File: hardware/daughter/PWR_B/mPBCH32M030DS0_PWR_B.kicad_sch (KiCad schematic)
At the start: 0 parts

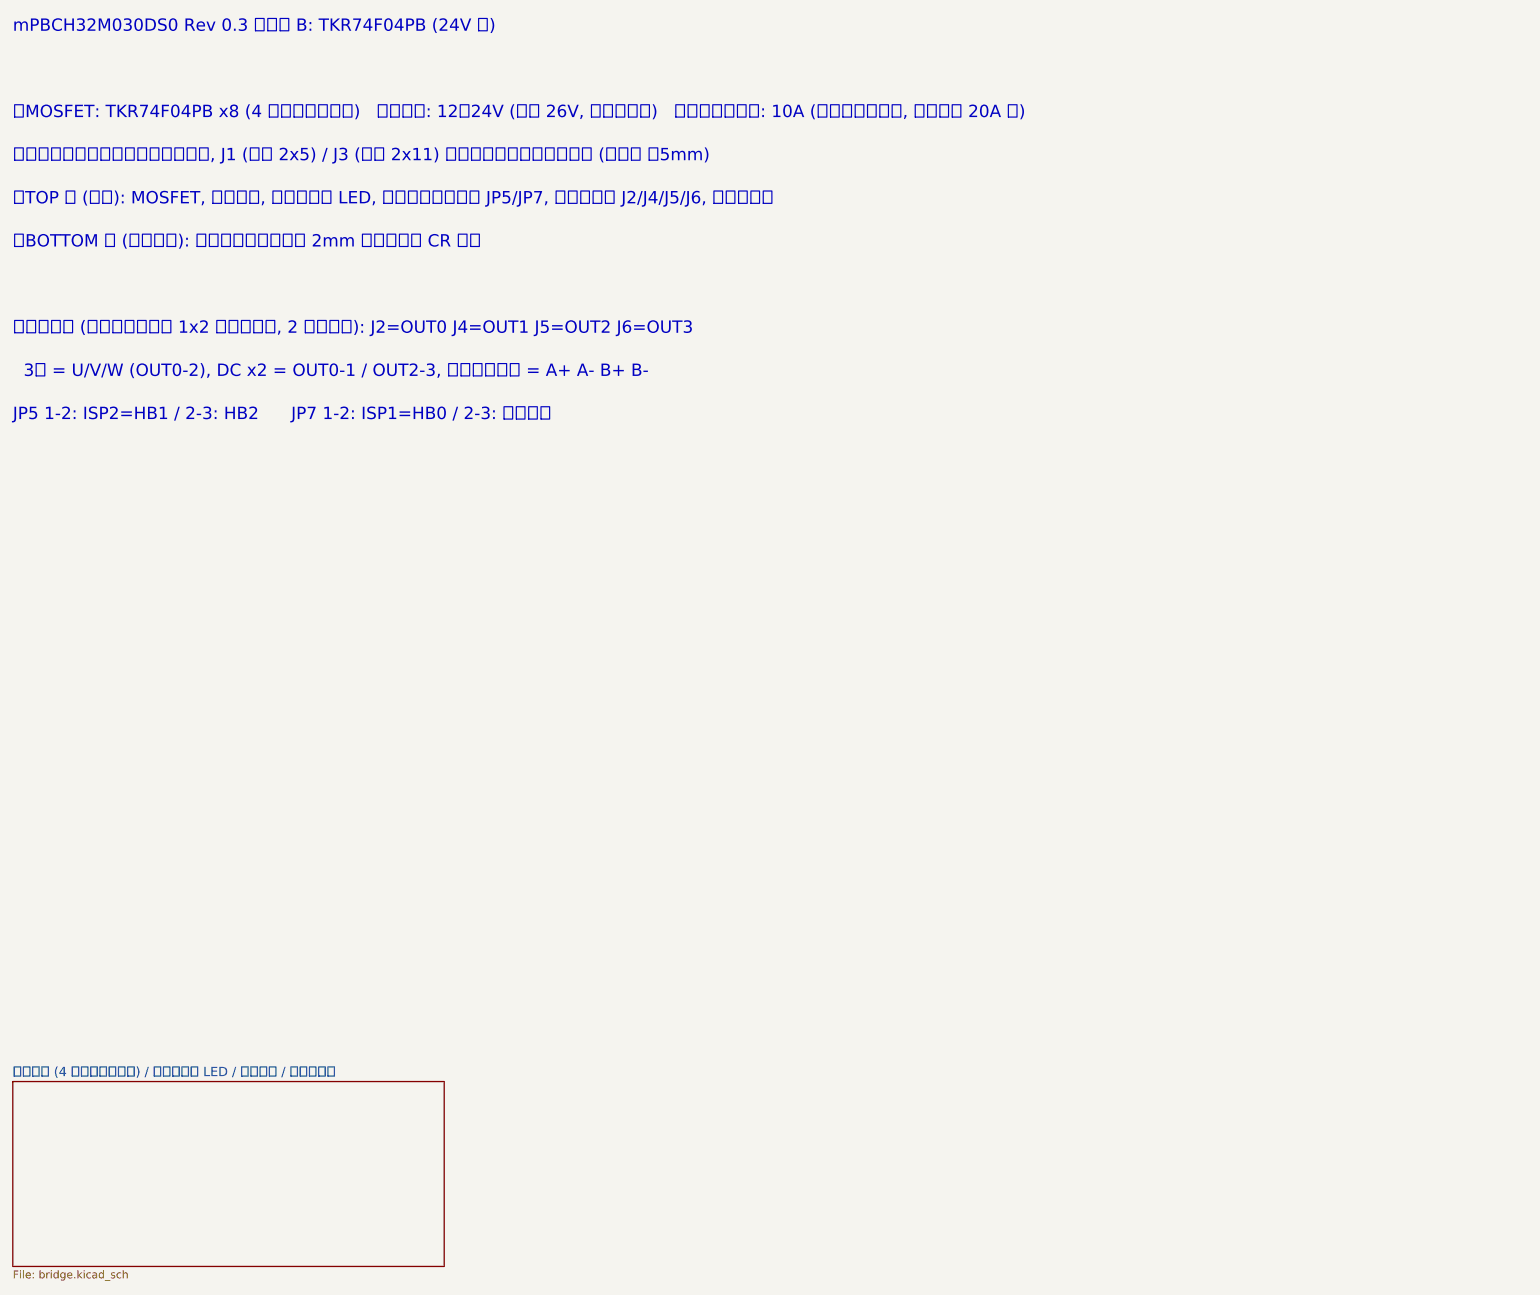
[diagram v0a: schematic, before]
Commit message: Rev 0.4: DIP-42 MCU module + power boards A/B/C (KiCad 8)
- MCU module: 20.32 x 53.34mm (8 x 21 grid), DIP-42 (0.6in rows), fits
  an 82 x 52mm breadboard. Headers can be fitted from either side;
  signal names on bottom silk. All LEDs (power, status, 8 gate LEDs) on
  the module top.
- Power boards take the module in two 1x21 sockets (left/right
  symmetric mating). FETs/shunts on the heatsink side, no LEDs.
  Voltage-dependent parts (TVS, OVP divider, bulk caps, BEMF divider)
  moved to the power boards. Breakout board D removed.
  A/C: 20.32 x 71.94mm, B (TO-263 x8): 40.64 x 66.94mm.
- Capacitors re-selected for realistic size vs voltage/capacitance
  (4.7uF 1608, 10uF/25V 2012, 10uF/50V 1206, 4.7nF/100V 1608, low
  profile electrolytics).
- Schematics and boards generated in KiCad 8 format; netlists verified
  with KiCad 8.0.9.
- Layout pipeline: Freerouting bridge (parallel), second pass, early
  repair before pours, island-aware maze repair, DRC via kicad-cli.
- DRC: power boards A/B/C have 0 unconnected / 0 electrical errors.
  The MCU module still has unrouted connections (work in progress).

Co-Authored-By: Claude Opus 5.5 <noreply@anthropic.com>
Claude-Session: https://claude.ai/code/session_01LENFjjhDfYjJZV1NWhB9uV
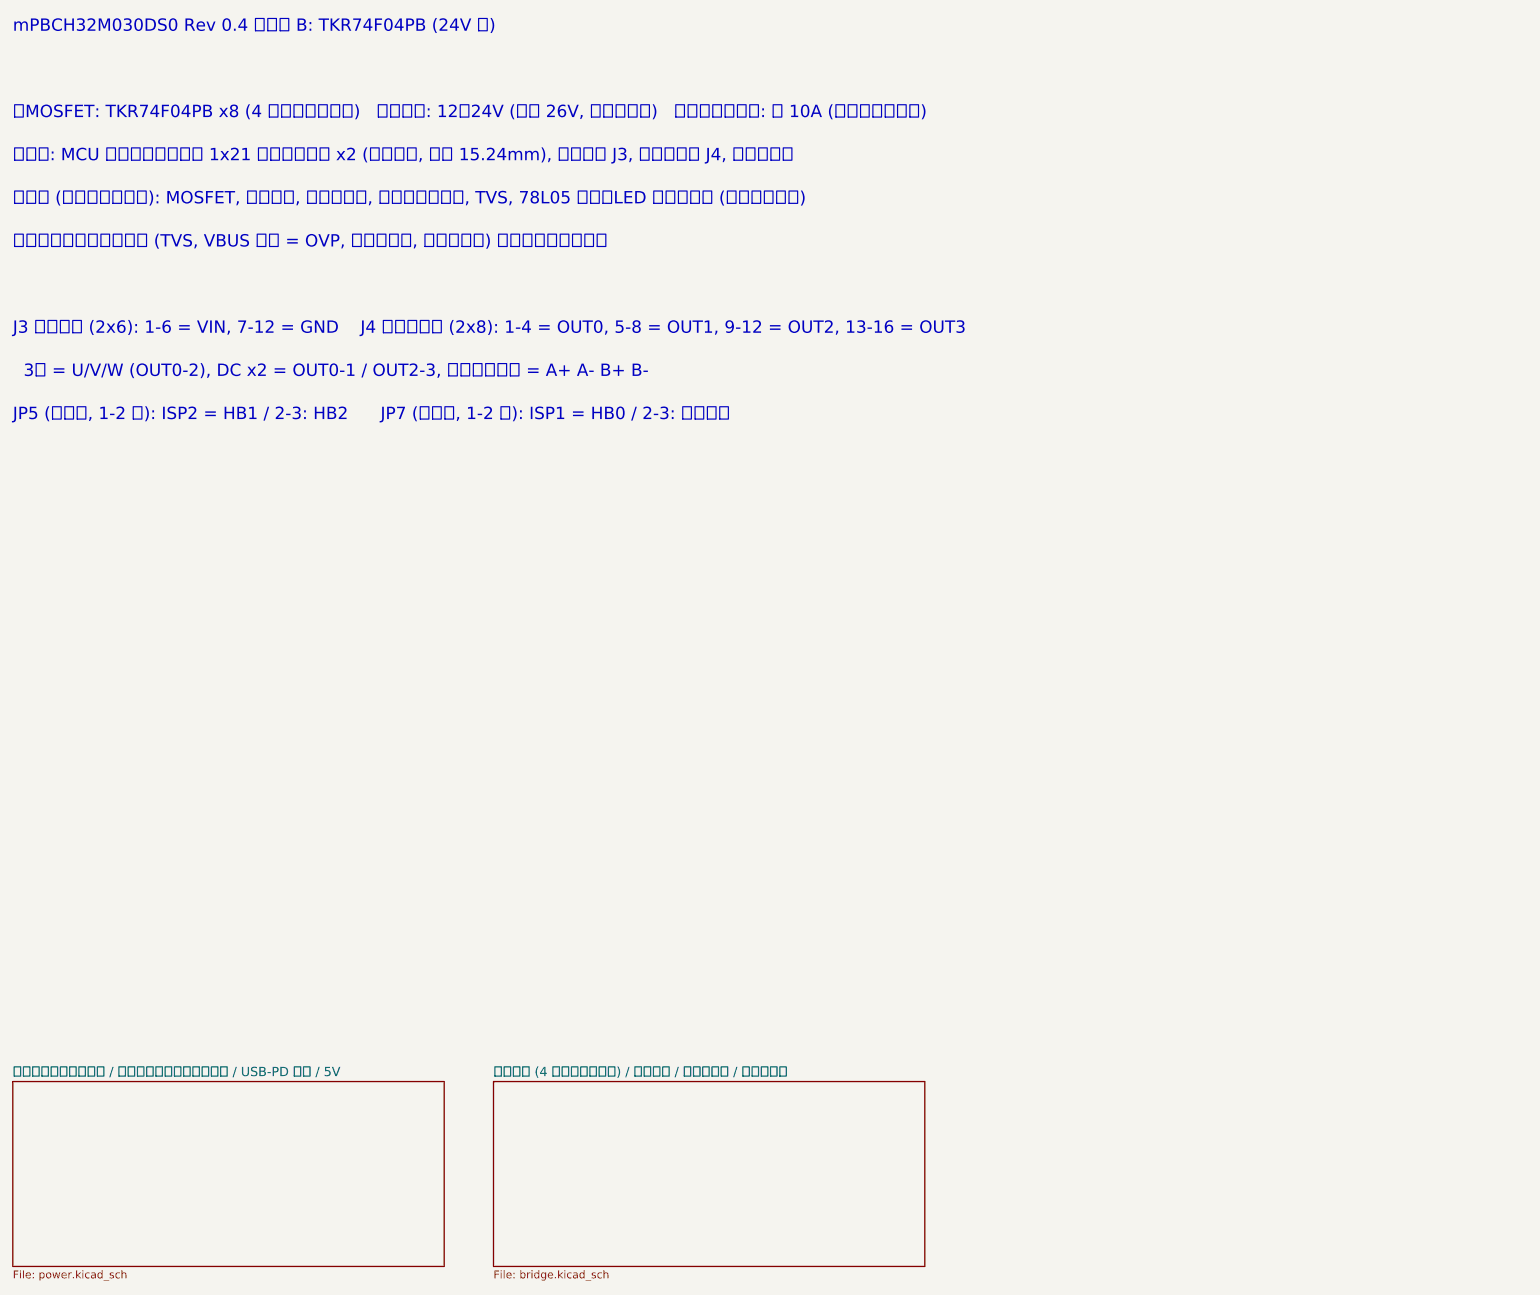
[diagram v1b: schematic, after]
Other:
- sheet パワー段 (4 ハーフブリッジ) / ゲート確認 LED / シャント / モータ出力 renamed パワー段 (4 ハーフブリッジ) / シャント / 相電圧分圧 / モータ出力
- added sheet モジュール用ソケット / 電源入力・理想ダイオード / USB-PD 経路 / 5V (power.kicad_sch)
- note added: "J3 電源入力 (2x6): 1-6 = VIN, 7-12 = GND J4 モータ出力 (2x8): 1-4 = OUT0, 5-8 = OUT1, 9-12 = OUT2, 13-16 = OUT3"
- note added: "JP5 (はんだ, 1-2 済): ISP2 = HB1 / 2-3: HB2 JP7 (はんだ, 1-2 済): ISP1 = HB0 / 2-3: バス電流"
- note added: "mPBCH32M030DS0 Rev 0.4 子基板 B: TKR74F04PB (24V 系)"
- note added: "・MOSFET: TKR74F04PB x8 (4 ハーフブリッジ) 入力電圧: 12〜24V (上限 26V, 安定化電源) 出力電流の目安: 約 10A (ピンヘッダ律速)"
- note added: "・上面: MCU モジュールを挿す 1x21 ピンソケット x2 (左右対称, 列間 15.24mm), 電源入力 J3, モータ出力 J4, バルク容量"
- note added: "・下面 (ヒートシンク側): MOSFET, シャント, ゲート抵抗, 理想ダイオード, TVS, 78L05 など。LED は置かない (モジュール側)"
- note added: "・電圧系に依存する部品 (TVS, VBUS 分圧 = OVP, バルク容量, 相電圧分圧) はこの基板で決める"
- note removed: "JP5 1-2: ISP2=HB1 / 2-3: HB2 JP7 1-2: ISP1=HB0 / 2-3: バス電流"
- note removed: "mPBCH32M030DS0 Rev 0.3 子基板 B: TKR74F04PB (24V 系)"
- note removed: "モータ出力 (各レッグ直近の 1x2 ピンヘッダ, 2 ピン並列): J2=OUT0 J4=OUT1 J5=OUT2 J6=OUT3"
- note removed: "・BOTTOM 面 (主基板側): ピンソケットと高さ 2mm 以下の小型 CR のみ"
- note removed: "・MOSFET: TKR74F04PB x8 (4 ハーフブリッジ) 入力電圧: 12〜24V (最大 26V, 安定化電源) 出力電流の目安: 10A (ピンヘッダ律速, 直付けで 20A 級)"
- note removed: "・TOP 面 (外側): MOSFET, シャント, ゲート確認 LED, 電流チャネル選択 JP5/JP7, モータ出力 J2/J4/J5/J6, バルク容量"
- note removed: "・主基板と裏面同士を向かい合わせ, J1 (電源 2x5) / J3 (信号 2x11) の裏面ピンソケットで接続 (基板間 約5mm)"
- title: mPBCH32M030DS0 Power daughter board B (TKR74F04PB) -> mPBCH32M030DS0 power board B (TKR74F04PB)
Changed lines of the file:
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@@
-(kicad_sch (version 20230121) (generator eeschema)
+(kicad_sch (version 20231120) (generator "eeschema") (generator_version "8.0")
 (paper "A3")
-(title_block (title "mPBCH32M030DS0 Power daughter board B (TKR74F04PB)") (date "2026-09-25") (rev "0.3") (company "ghostinkoma") (comment 1 "トップシート / 仕様概要") (comment 2 "個人利用可 (クレジット表示必須) / 商用利用は要連絡 / 無保証  -  LICENSE 参照"))
-(text "mPBCH32M030DS0 Rev 0.3 子基板 B: TKR74F04PB (24V 系)" (at 20 30 0) (effects (font (size 2 2)) (justify left bottom)))
-(text "" (at 20 37 0) (effects (font (size 2 2)) (justify left bottom)))
-(text "・MOSFET: TKR74F04PB x8 (4 ハーフブリッジ)   入力電圧: 12〜24V (最大 26V, 安定化電源)   出力電流の目安: 10A (ピンヘッダ律速, 直付けで 20A 級)" (at 20 44 0) (effects (font (size 2 2)) (justify left bottom)))
-(text "・主基板と裏面同士を向かい合わせ, J1 (電源 2x5) / J3 (信号 2x11) の裏面ピンソケットで接続 (基板間 約5mm)" (at 20 51 0) (effects (font (size 2 2)) (justify left bottom)))
-(text "・TOP 面 (外側): MOSFET, シャント, ゲート確認 LED, 電流チャネル選択 JP5/JP7, モータ出力 J2/J4/J5/J6, バルク容量" (at 20 58 0) (effects (font (size 2 2)) (justify left bottom)))
-(text "・BOTTOM 面 (主基板側): ピンソケットと高さ 2mm 以下の小型 CR のみ" (at 20 65 0) (effects (font (size 2 2)) (justify left bottom)))
-(text "" (at 20 72 0) (effects (font (size 2 2)) (justify left bottom)))
-(text "モータ出力 (各レッグ直近の 1x2 ピンヘッダ, 2 ピン並列): J2=OUT0 J4=OUT1 J5=OUT2 J6=OUT3" (at 20 79 0) (effects (font (size 2 2)) (justify left bottom)))
-(text "  3相 = U/V/W (OUT0-2), DC x2 = OUT0-1 / OUT2-3, ステッピング = A+ A- B+ B-" (at 20 86 0) (effects (font (size 2 2)) (justify left bottom)))
-(text "JP5 1-2: ISP2=HB1 / 2-3: HB2      JP7 1-2: ISP1=HB0 / 2-3: バス電流" (at 20 93 0) (effects (font (size 2 2)) (justify left bottom)))
-(sheet (at 20 200) (size 70 30) (fields_autoplaced) (stroke (width 0.1524) (type solid)) (fill (color 0 0 0 0.0000))
-(property "Sheetname" "パワー段 (4 ハーフブリッジ) / ゲート確認 LED / シャント / モータ出力" (at 20 199.3 0) (effects (font (size 1.5 1.5)) (justify left bottom)))
-(property "Sheetfile" "bridge.kicad_sch" (at 20 230.6 0) (effects (font (size 1.27 1.27)) (justify left top)))
+(title_block (title "mPBCH32M030DS0 power board B (TKR74F04PB)") (date "2026-09-26") (rev "0.4") (company "ghostinkoma") (comment 1 "トップシート / 仕様概要") (comment 2 "個人利用可 (クレジット表示必須) / 商用利用は要連絡 / 無保証  -  LICENSE 参照"))
+(text "mPBCH32M030DS0 Rev 0.4 子基板 B: TKR74F04PB (24V 系)" (exclude_from_sim no) (at 20 30 0) (effects (font (size 2 2)) (justify left bottom)))
+(text "" (exclude_from_sim no) (at 20 37 0) (effects (font (size 2 2)) (justify left bottom)))
+(text "・MOSFET: TKR74F04PB x8 (4 ハーフブリッジ)   入力電圧: 12〜24V (上限 26V, 安定化電源)   出力電流の目安: 約 10A (ピンヘッダ律速)" (exclude_from_sim no) (at 20 44 0) (effects (font (size 2 2)) (justify left bottom)))
+(text "・上面: MCU モジュールを挿す 1x21 ピンソケット x2 (左右対称, 列間 15.24mm), 電源入力 J3, モータ出力 J4, バルク容量" (exclude_from_sim no) (at 20 51 0) (effects (font (size 2 2)) (justify left bottom)))
+(text "・下面 (ヒートシンク側): MOSFET, シャント, ゲート抵抗, 理想ダイオード, TVS, 78L05 など。LED は置かない (モジュール側)" (exclude_from_sim no) (at 20 58 0) (effects (font (size 2 2)) (justify left bottom)))
+(text "・電圧系に依存する部品 (TVS, VBUS 分圧 = OVP, バルク容量, 相電圧分圧) はこの基板で決める" (exclude_from_sim no) (at 20 65 0) (effects (font (size 2 2)) (justify left bottom)))
+(text "" (exclude_from_sim no) (at 20 72 0) (effects (font (size 2 2)) (justify left bottom)))
+(text "J3 電源入力 (2x6): 1-6 = VIN, 7-12 = GND    J4 モータ出力 (2x8): 1-4 = OUT0, 5-8 = OUT1, 9-12 = OUT2, 13-16 = OUT3" (exclude_from_sim no) (at 20 79 0) (effects (font (size 2 2)) (justify left bottom)))
+(text "  3相 = U/V/W (OUT0-2), DC x2 = OUT0-1 / OUT2-3, ステッピング = A+ A- B+ B-" (exclude_from_sim no) (at 20 86 0) (effects (font (size 2 2)) (justify left bottom)))
+(text "JP5 (はんだ, 1-2 済): ISP2 = HB1 / 2-3: HB2      JP7 (はんだ, 1-2 済): ISP1 = HB0 / 2-3: バス電流" (exclude_from_sim no) (at 20 93 0) (effects (font (size 2 2)) (justify left bottom)))
+(sheet (at 20 200) (size 70 30) (fields_autoplaced yes) (stroke (width 0.1524) (type solid)) (fill (color 0 0 0 0.0000))
+(property "Sheetname" "モジュール用ソケット / 電源入力・理想ダイオード / USB-PD 経路 / 5V" (at 20 199.3 0) (effects (font (size 1.5 1.5)) (justify left bottom)))
+(property "Sheetfile" "power.kicad_sch" (at 20 230.6 0) (effects (font (size 1.27 1.27)) (justify left top)))
 (instances (project "mPBCH32M030DS0_PWR_B" (path "/33cf0c15-e463-5f39-b895-a96f9ee80b86" (page "2"))))
 )
+(sheet (at 98 200) (size 70 30) (fields_autoplaced yes) (stroke (width 0.1524) (type solid)) (fill (color 0 0 0 0.0000))
+(property "Sheetname" "パワー段 (4 ハーフブリッジ) / シャント / 相電圧分圧 / モータ出力" (at 98 199.3 0) (effects (font (size 1.5 1.5)) (justify left bottom)))
+(property "Sheetfile" "bridge.kicad_sch" (at 98 230.6 0) (effects (font (size 1.27 1.27)) (justify left top)))
+(instances (project "mPBCH32M030DS0_PWR_B" (path "/33cf0c15-e463-5f39-b895-a96f9ee80b86" (page "3"))))
+)
 (sheet_instances (path "/" (page "1")))

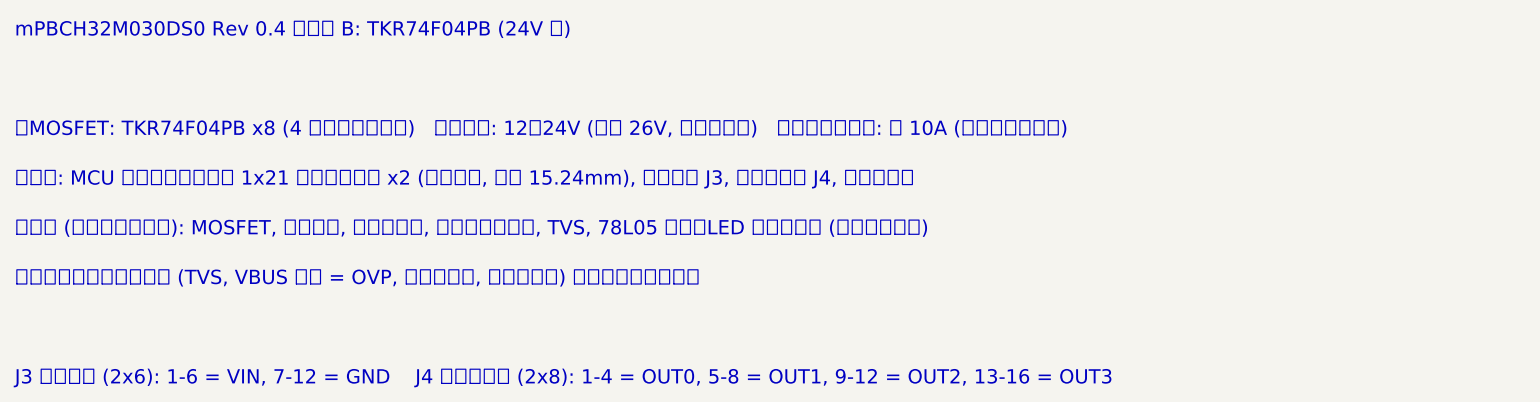
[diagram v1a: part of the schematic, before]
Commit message: 9マス版に一本化 (8マス版を削除)
- 8 マス版 (20.32mm) は JLCPCB の 2 層標準 0.127mm で配線しきれないため削除
- 9 マス版 (22.86mm, 端子列 0.7in) を hardware/ 直下・hardware/daughter/・hardware/fab/・docs/pcb/ へ移動
- ベタなし版は hardware/nopour/ (図は docs/pcb/nopour/)
- gen_pcb.py から MPB_W9 の切り替えを外し 9 マス固定に。既定ルールは 0.127mm / ビア 0.6/0.3
  (再生成した配置が確定済みの 4 基板と一致することを確認)
- 回路図の注記 (外形・列間) を 22.86mm / 17.78mm に更新し PDF を再出力
- README / stacking.md / design.md を 9 マス版のみの記述に更新

Co-Authored-By: Claude Opus 5.5 <noreply@anthropic.com>
Claude-Session: https://claude.ai/code/session_01LENFjjhDfYjJZV1NWhB9uV
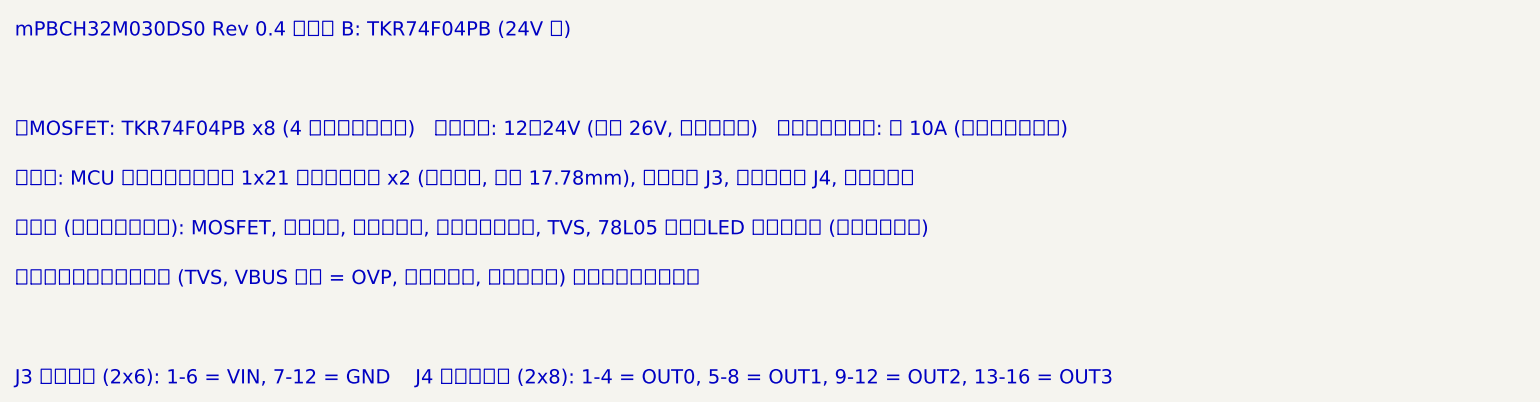
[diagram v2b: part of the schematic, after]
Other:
- note added: "・上面: MCU モジュールを挿す 1x21 ピンソケット x2 (左右対称, 列間 17.78mm), 電源入力 J3, モータ出力 J4, バルク容量"
- note removed: "・上面: MCU モジュールを挿す 1x21 ピンソケット x2 (左右対称, 列間 15.24mm), 電源入力 J3, モータ出力 J4, バルク容量"
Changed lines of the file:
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@@
 (text "" (exclude_from_sim no) (at 20 37 0) (effects (font (size 2 2)) (justify left bottom)))
 (text "・MOSFET: TKR74F04PB x8 (4 ハーフブリッジ)   入力電圧: 12〜24V (上限 26V, 安定化電源)   出力電流の目安: 約 10A (ピンヘッダ律速)" (exclude_from_sim no) (at 20 44 0) (effects (font (size 2 2)) (justify left bottom)))
-(text "・上面: MCU モジュールを挿す 1x21 ピンソケット x2 (左右対称, 列間 15.24mm), 電源入力 J3, モータ出力 J4, バルク容量" (exclude_from_sim no) (at 20 51 0) (effects (font (size 2 2)) (justify left bottom)))
+(text "・上面: MCU モジュールを挿す 1x21 ピンソケット x2 (左右対称, 列間 17.78mm), 電源入力 J3, モータ出力 J4, バルク容量" (exclude_from_sim no) (at 20 51 0) (effects (font (size 2 2)) (justify left bottom)))
 (text "・下面 (ヒートシンク側): MOSFET, シャント, ゲート抵抗, 理想ダイオード, TVS, 78L05 など。LED は置かない (モジュール側)" (exclude_from_sim no) (at 20 58 0) (effects (font (size 2 2)) (justify left bottom)))
 (text "・電圧系に依存する部品 (TVS, VBUS 分圧 = OVP, バルク容量, 相電圧分圧) はこの基板で決める" (exclude_from_sim no) (at 20 65 0) (effects (font (size 2 2)) (justify left bottom)))
